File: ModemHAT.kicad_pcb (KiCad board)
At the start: 2 copper layers, 85 x 56.5 mm, 104 parts, among them J1 RJ11, J2 2x20 0.1" Stacking Header, J3 8R, Q1 NPN 300V 0.5A, Q2 PNP 300V 0.5A, Q3 NPN 300V 0.5A, Q4 NPN 80V 330mW, Q5 NPN 80V 330mW, SW1 SW_SPDT, U1 Si2457-D-FT, U2 Si3018-F-GS, U3 74LVC541, U4 LM4819, U5 24LC32, U6 25LC320, Y1 32.768kHz 25ppm

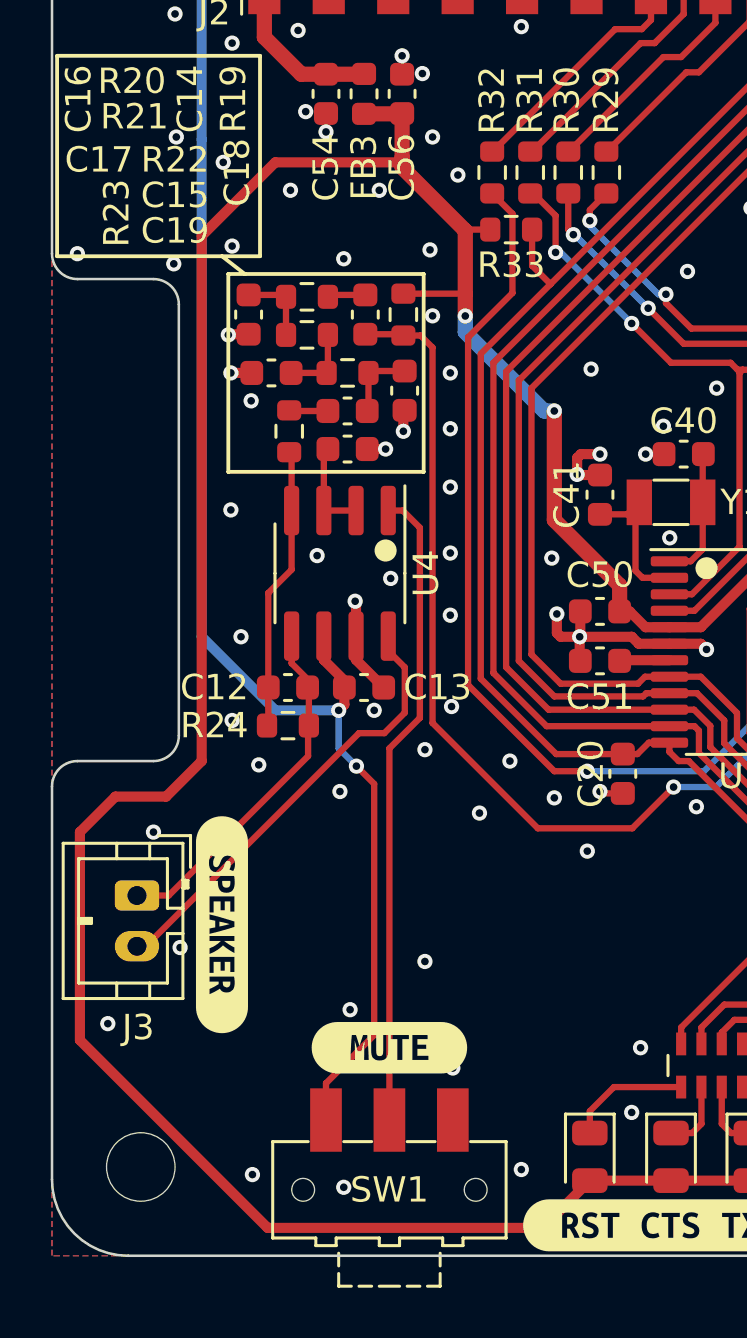
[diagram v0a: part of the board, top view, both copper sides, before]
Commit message: move trace away from mounting hole
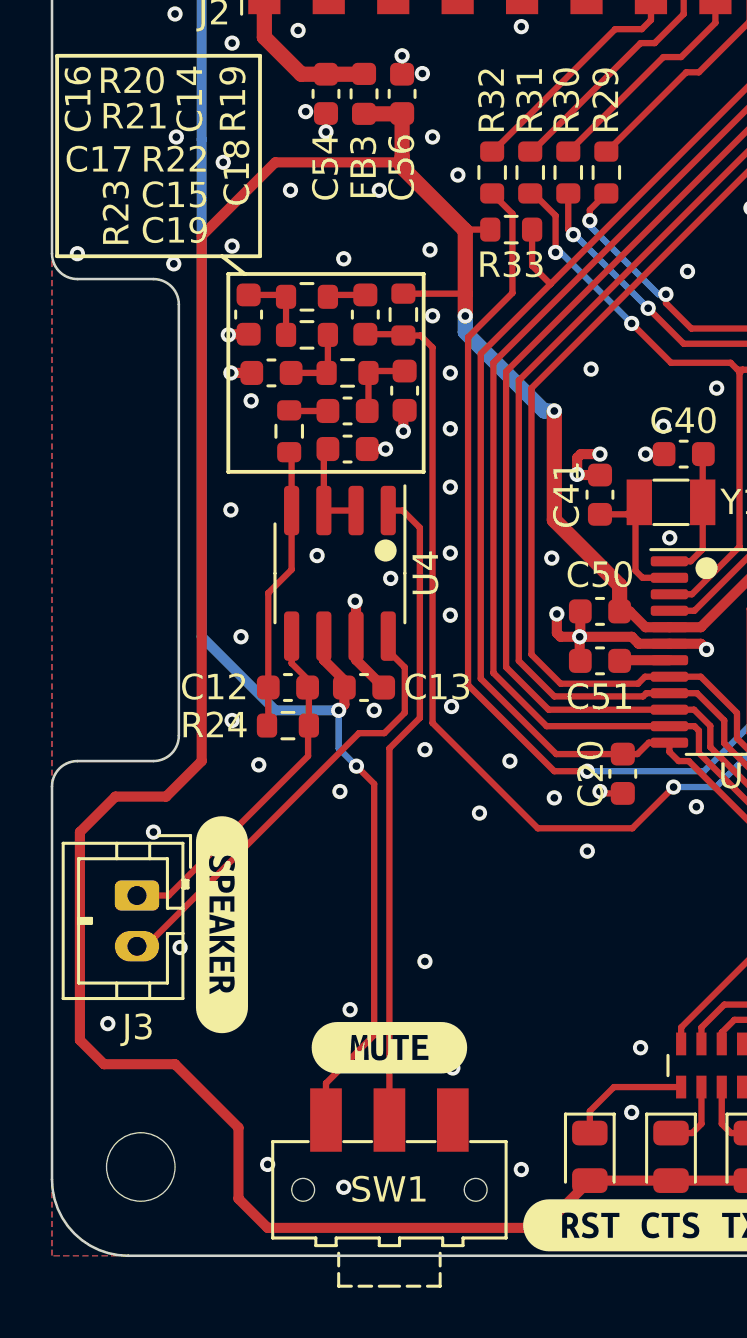
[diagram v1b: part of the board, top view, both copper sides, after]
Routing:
- net +3V3: track 186.4 -> 188.1 mm
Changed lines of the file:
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@@
   (via (at 87.05 85.2) (size 0.6) (drill 0.3) (layers "F.Cu" "B.Cu") (net 6))
   (via (at 81 69.9) (size 0.6) (drill 0.3) (layers "F.Cu" "B.Cu") (free) (net 6))
-  (via (at 87.9 116.8) (size 0.6) (drill 0.3) (layers "F.Cu" "B.Cu") (free) (net 6))
+  (via (at 88.5 116.4) (size 0.6) (drill 0.3) (layers "F.Cu" "B.Cu") (free) (net 6))
   (via (at 136.65 71.75) (size 0.6) (drill 0.3) (layers "F.Cu" "B.Cu") (free) (net 6))
   (via (at 89.7 71.7) (size 0.6) (drill 0.3) (layers "F.Cu" "B.Cu") (free) (net 6))
@@
   (segment (start 131.875 100.635) (end 134.335 100.635) (width 0.4) (layer "F.Cu") (net 39))
   (segment (start 134.75 101.05) (end 135.4 101.05) (width 0.4) (layer "F.Cu") (net 39))
-  (segment (start 85.9 100.5) (end 85.9 79.8) (width 0.4) (layer "F.Cu") (net 40))
+  (segment (start 88.8 76.9) (end 85.9 79.8) (width 0.4) (layer "F.Cu") (net 40))
   (segment (start 111.975 90.825) (end 112 90.8) (width 0.4) (layer "F.Cu") (net 40))
   (segment (start 102.772463 94.6) (end 102.375 94.6) (width 0.4) (layer "F.Cu") (net 40))
@@
   (segment (start 105.575 95.225) (end 109.2 91.6) (width 0.4) (layer "F.Cu") (net 40))
   (segment (start 120.725 75.775) (end 121.5375 75.775) (width 0.4) (layer "F.Cu") (net 40))
+  (segment (start 84.85 112.45) (end 87.35 114.95) (width 0.4) (layer "F.Cu") (net 40))
   (segment (start 96.331444 79.55) (end 96.290722 79.590722) (width 0.25) (layer "F.Cu") (net 40))
-  (segment (start 101.2 117.0375) (end 99.3375 118.9) (width 0.4) (layer "F.Cu") (net 40))
   (segment (start 115.675 85.1125) (end 115.6625 85.125) (width 0.4) (layer "F.Cu") (net 40))
   (segment (start 97.275 79.55) (end 96.331444 79.55) (width 0.25) (layer "F.Cu") (net 40))
-  (segment (start 85.9 79.8) (end 88.8 76.9) (width 0.4) (layer "F.Cu") (net 40))
-  (segment (start 81.1 111.5) (end 81.1 103.3) (width 0.4) (layer "F.Cu") (net 40))
+  (segment (start 81.1 103.3) (end 81.1 111.5) (width 0.4) (layer "F.Cu") (net 40))
+  (segment (start 99.3375 118.9) (end 101.2 117.0375) (width 0.4) (layer "F.Cu") (net 40))
   (segment (start 118.275 74.8) (end 119.775 76.3) (width 0.25) (layer "F.Cu") (net 40))
+  (segment (start 87.35 117.75) (end 88.5 118.9) (width 0.4) (layer "F.Cu") (net 40))
   (segment (start 109.9375 86.425) (end 108.5 86.425) (width 0.25) (layer "F.Cu") (net 40))
   (segment (start 104.3375 95.225) (end 105.575 95.225) (width 0.4) (layer "F.Cu") (net 40))
   (segment (start 92.3 74.9875) (end 93.7875 74.9875) (width 0.6) (layer "F.Cu") (net 40))
   (segment (start 96.290722 79.590722) (end 96.290722 82.090722) (width 0.6) (layer "F.Cu") (net 40))
-  (segment (start 93.6 76.9) (end 93.8 76.7) (width 0.4) (layer "F.Cu") (net 40))
   (segment (start 93.7875 74.9875) (end 93.8 74.975) (width 0.6) (layer "F.Cu") (net 40))
   (segment (start 111.975 94.2) (end 111.975 90.825) (width 0.4) (layer "F.Cu") (net 40))
@@
   (segment (start 117.3 83.6) (end 115.675 83.6) (width 0.4) (layer "F.Cu") (net 40))
   (segment (start 115.075 107.75) (end 115.6 108.275) (width 0.25) (layer "F.Cu") (net 40))
+  (segment (start 93.8 76.7) (end 93.6 76.9) (width 0.4) (layer "F.Cu") (net 40))
   (segment (start 96.290722 82.090722) (end 96.290722 82.95539) (width 0.6) (layer "F.Cu") (net 40))
   (segment (start 96.275 82.075) (end 93.85 82.075) (width 0.25) (layer "F.Cu") (net 40))
   (segment (start 111.832881 86.425) (end 112.85 87.442119) (width 0.25) (layer "F.Cu") (net 40))
-  (segment (start 99.3375 118.9) (end 88.5 118.9) (width 0.4) (layer "F.Cu") (net 40))
+  (segment (start 81.1 111.5) (end 82.05 112.45) (width 0.4) (layer "F.Cu") (net 40))
   (segment (start 116.4 108.2) (end 115.675 108.2) (width 0.4) (layer "F.Cu") (net 40))
   (segment (start 96.290722 82.090722) (end 96.275 82.075) (width 0.25) (layer "F.Cu") (net 40))
   (segment (start 109.9375 86.425) (end 111.832881 86.425) (width 0.25) (layer "F.Cu") (net 40))
-  (segment (start 84.5 101.9) (end 85.9 100.5) (width 0.4) (layer "F.Cu") (net 40))
   (segment (start 119.775 78.325) (end 119.775 76.3) (width 0.4) (layer "F.Cu") (net 40))
   (segment (start 112.85 87.442119) (end 112.85 90.85) (width 0.25) (layer "F.Cu") (net 40))
-  (segment (start 81.1 103.3) (end 82.5 101.9) (width 0.4) (layer "F.Cu") (net 40))
   (segment (start 123.48 117.0375) (end 120.3 117.0375) (width 0.4) (layer "F.Cu") (net 40))
   (segment (start 103.397463 95.225) (end 102.772463 94.6) (width 0.4) (layer "F.Cu") (net 40))
   (segment (start 112 90.8) (end 112.9 90.8) (width 0.4) (layer "F.Cu") (net 40))
+  (segment (start 84.5 101.9) (end 82.5 101.9) (width 0.4) (layer "F.Cu") (net 40))
   (segment (start 102.375 94.6) (end 102.375 93.575) (width 0.6) (layer "F.Cu") (net 40))
   (segment (start 116.1 90.8) (end 117.3 89.6) (width 0.4) (layer "F.Cu") (net 40))
@@
   (segment (start 116.1 90.8) (end 112.9 90.8) (width 0.4) (layer "F.Cu") (net 40))
   (segment (start 93.8 74.975) (end 93.8 76.7) (width 0.6) (layer "F.Cu") (net 40))
+  (segment (start 87.35 114.95) (end 87.35 117.75) (width 0.4) (layer "F.Cu") (net 40))
   (segment (start 117.3 89.6) (end 117.3 83.6) (width 0.4) (layer "F.Cu") (net 40))
+  (segment (start 85.9 79.8) (end 85.9 100.5) (width 0.4) (layer "F.Cu") (net 40))
   (segment (start 117.3 80.8) (end 119.775 78.325) (width 0.4) (layer "F.Cu") (net 40))
   (segment (start 104.3375 95.225) (end 103.397463 95.225) (width 0.4) (layer "F.Cu") (net 40))
+  (segment (start 93.6 76.9) (end 88.8 76.9) (width 0.4) (layer "F.Cu") (net 40))
   (segment (start 120.2 76.3) (end 120.725 75.775) (width 0.4) (layer "F.Cu") (net 40))
+  (segment (start 88.5 118.9) (end 99.3375 118.9) (width 0.4) (layer "F.Cu") (net 40))
   (segment (start 102.375 93.575) (end 99.8 91) (width 0.6) (layer "F.Cu") (net 40))
-  (segment (start 82.5 101.9) (end 84.5 101.9) (width 0.4) (layer "F.Cu") (net 40))
   (segment (start 110.0625 94.575) (end 111.175 94.575) (width 0.4) (layer "F.Cu") (net 40))
-  (segment (start 88.8 76.9) (end 93.6 76.9) (width 0.4) (layer "F.Cu") (net 40))
   (segment (start 115.6625 85.775) (end 115.6625 85.125) (width 0.25) (layer "F.Cu") (net 40))
   (segment (start 111.55 94.2) (end 111.975 94.2) (width 0.4) (layer "F.Cu") (net 40))
@@
   (segment (start 96.290722 79.590722) (end 93.8 77.1) (width 0.6) (layer "F.Cu") (net 40))
   (segment (start 118.175 74.8) (end 118.275 74.8) (width 0.25) (layer "F.Cu") (net 40))
+  (segment (start 82.5 101.9) (end 81.1 103.3) (width 0.4) (layer "F.Cu") (net 40))
   (segment (start 99.8 91) (end 99.8 86.7) (width 0.6) (layer "F.Cu") (net 40))
+  (segment (start 82.05 112.45) (end 84.85 112.45) (width 0.4) (layer "F.Cu") (net 40))
   (segment (start 109.2 91.6) (end 110 90.8) (width 0.4) (layer "F.Cu") (net 40))
   (segment (start 108.5 86.425) (end 108.2 86.725) (width 0.25) (layer "F.Cu") (net 40))
-  (segment (start 88.5 118.9) (end 81.1 111.5) (width 0.4) (layer "F.Cu") (net 40))
+  (segment (start 85.9 100.5) (end 84.5 101.9) (width 0.4) (layer "F.Cu") (net 40))
   (via (at 96.290722 82.95539) (size 0.6) (drill 0.3) (layers "F.Cu" "B.Cu") (net 40))
   (via (at 118.7625 117.0375) (size 0.6) (drill 0.3) (layers "F.Cu" "B.Cu") (net 40))
